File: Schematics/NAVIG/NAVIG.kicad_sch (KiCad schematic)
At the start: 19 parts, among them J12 GNSS_SMA, U11 BMP390, U4 BNO055, U4 STM32F205RETx, U7 NEO-M9N, Y2 32.768KHz

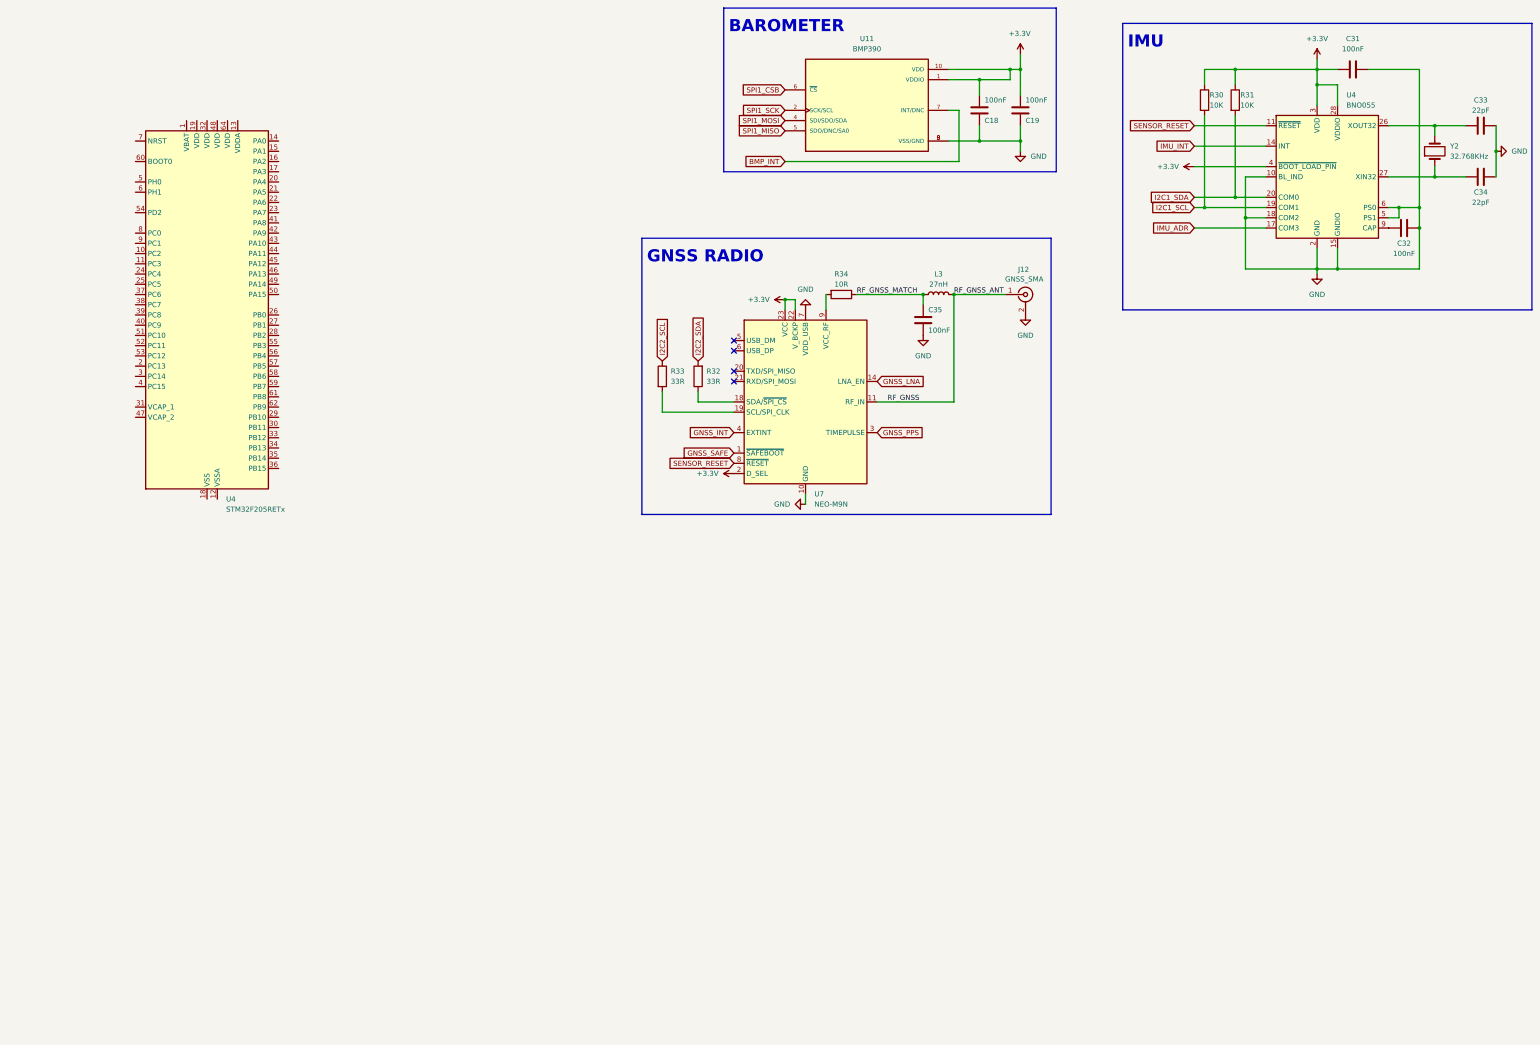
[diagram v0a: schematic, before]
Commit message: navig board pcb and schematic along with cntrl board edits
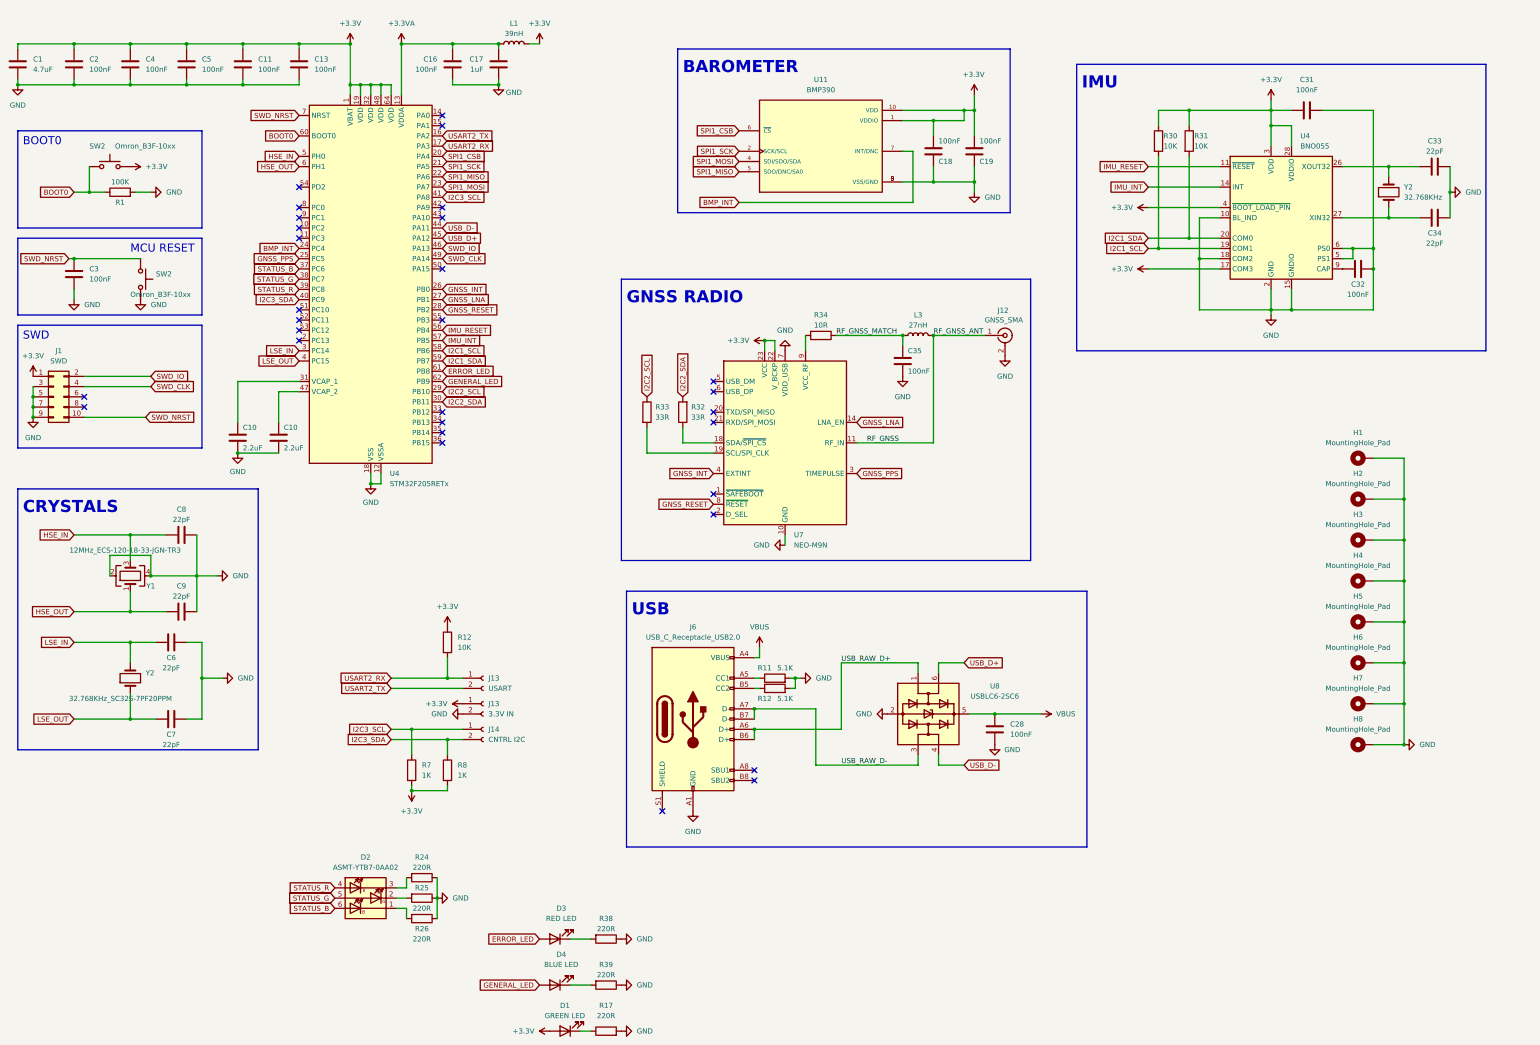
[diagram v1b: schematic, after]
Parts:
- added C1: 4.7uF, Capacitor_SMD:C_0603_1608Metric, symbol Device:C
- added C10 (x2): 2.2uF, Capacitor_SMD:C_0603_1608Metric, symbol Device:C
- added C11, C13, C16, C2, C28, C3, C4, C5: 100nF, Capacitor_SMD:C_0603_1608Metric, symbol Device:C
- added C17: 1uF, Capacitor_SMD:C_0603_1608Metric, symbol Device:C
- added C6, C7, C8, C9: 22pF, Capacitor_SMD:C_0603_1608Metric, symbol Device:C
- added D1: GREEN LED, LED_SMD:LED_0603_1608Metric, symbol Device:LED
- added D2: ASMT-YTB7-0AA02, LED_SMD:LED_Avago_PLCC6_3x2.8mm, symbol LED:ASMT-YTB7-0AA02
- added D3: RED LED, LED_SMD:LED_0603_1608Metric, symbol Device:LED
- added D4: BLUE LED, LED_SMD:LED_0603_1608Metric, symbol Device:LED
- added H1, H2, H3, H4, H5, H6, H7, H8: MountingHole_Pad, MountingHole:MountingHole_2.2mm_M2_Pad_TopBottom, symbol Mechanical:MountingHole_Pad
- added J1: SWD, Connector_PinHeader_1.27mm:PinHeader_2x05_P1.27mm_Vertical_SMD, symbol Connector_Generic:Conn_02x05_Odd_Even
- added J13: USART, Connector_JST:JST_XH_B2B-XH-A_1x02_P2.50mm_Vertical, symbol Connector:Conn_01x02_Socket
- added J13: 3.3V IN, Connector_JST:JST_XH_B2B-XH-A_1x02_P2.50mm_Vertical, symbol Connector:Conn_01x02_Socket
- added J14: CNTRL I2C, Connector_JST:JST_XH_B2B-XH-A_1x02_P2.50mm_Vertical, symbol Connector:Conn_01x02_Socket
- added J6: USB_C_Receptacle_USB2.0, Connector_USB:USB_C_Receptacle_GCT_USB4105-xx-A_16P_TopMnt_Horizontal, symbol Connector:USB_C_Receptacle_USB2.0
- added L1: 39nH, Inductor_SMD:L_0603_1608Metric, symbol Device:L
- added R1: 100K, Resistor_SMD:R_0603_1608Metric, symbol Device:R
- added R11, R12: 5.1K, Resistor_SMD:R_0603_1608Metric, symbol Device:R
- added R12: 10K, Resistor_SMD:R_0603_1608Metric, symbol Device:R
- added R17, R24, R25, R26, R38, R39: 220R, Resistor_SMD:R_0603_1608Metric, symbol Device:R
- added R7, R8: 1K, Resistor_SMD:R_0603_1608Metric, symbol Device:R
- added SW2 (x2): Omron_B3F-10xx, Button_Switch_THT:SW_TH_Tactile_Omron_B3F-10xx, symbol Switch:SW_Push
- added U8: USBLC6-2SC6, Package_TO_SOT_SMD:SOT-23-6, symbol Power_Protection:USBLC6-2SC6
- added Y1: 12MHz_ECS-120-18-33-JGN-TR3, Crystal:Crystal_SMD_3225-4Pin_3.2x2.5mm, symbol Device:Crystal_GND24
- added Y2: 32.768KHz_SC32S-7PF20PPM, Crystal:Crystal_SMD_3215-2Pin_3.2x1.5mm, symbol Device:Crystal
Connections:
- net IMU_ADR is gone; now on net +3.3V: U4.17 (COM3)
- net +3.3V: now also U4.1 (VBAT), U4.19 (VDD), U4.32 (VDD), U4.48 (VDD), U4.64 (VDD), C1.1, C11.1, C13.1, C2.1, C4.1, C5.1, D1.2 (A), J1.1 (Pin_1), J13.1 (Pin_1), L1.1, R12.1, R7.2, R8.2, SW2.2; no longer U7.2 (D_SEL)
- net BMP_INT: now also U4.24 (PC4)
- net GND: now also U4.12 (VSSA), U4.18 (VSS), U4.63 (VSS), C1.2, C10.1, C10.1, C11.2, C13.2, C16.2, C17.2, C2.2, C28.2, C3.2, C4.2, C5.2, C6.2, C7.2, C8.1, C9.2, H1.1, H2.1, H3.1, H4.1, H5.1, H6.1, H7.1, H8.1, J1.3 (Pin_3), J1.5 (Pin_5), J1.7 (Pin_7), J1.9 (Pin_9), J13.2 (Pin_2), J6.A1 (GND), J6.A12 (GND), J6.B1 (GND), J6.B12 (GND), R1.2, R11.2, R12.2, R17.2, R24.1, R25.1, R26.1, R38.1, R39.1, SW2.2, U8.2 (GND), Y1.2, Y1.4
- net GNSS_INT: now also U4.26 (PB0)
- net GNSS_LNA: now also U4.27 (PB1)
- net GNSS_PPS: now also U4.25 (PC5)
- net I2C1_SCL: now also U4.58 (PB6)
- net I2C1_SDA: now also U4.59 (PB7)
- net I2C2_SCL: now also U4.29 (PB10)
- net I2C2_SDA: now also U4.30 (PB11)
- net IMU_INT: now also U4.57 (PB5)
- net SPI1_CSB: now also U4.20 (PA4)
- net SPI1_MISO: now also U4.22 (PA6)
- net SPI1_MOSI: now also U4.23 (PA7)
- net SPI1_SCK: now also U4.21 (PA5)
- net +3.3VA: now reaches U4.13 (VDDA)
- net +3.3VA: now also C16.1, C17.1, L1.2
- net USART2_TX: now reaches U4.16 (PA2)
- net USART2_TX: now also J13.2 (Pin_2)
- net USART2_RX: now reaches U4.17 (PA3)
- net USART2_RX: now also J13.1 (Pin_1), R12.2
- net GNSS_RESET: now reaches U4.28 (PB2)
- net GNSS_RESET: now also U7.8 (~{RESET})
- net LSE_IN: now reaches U4.3 (PC14)
- net LSE_IN: now also C6.1, Y2.2
- net at U4.31 (VCAP_1): now also C10.2
- net STATUS_B: now reaches U4.37 (PC6)
- net STATUS_B: now also D2.6 (AB)
- net STATUS_G: now reaches U4.38 (PC7)
- net STATUS_G: now also D2.5 (AG)
- net STATUS_R: now reaches U4.39 (PC8)
- net STATUS_R: now also D2.4 (AR)
- net LSE_OUT: now reaches U4.4 (PC15)
- net LSE_OUT: now also C7.1, Y2.1
- net I2C3_SDA: now reaches U4.40 (PC9)
- net I2C3_SDA: now also J14.2 (Pin_2), R8.1
- net I2C3_SCL: now reaches U4.41 (PA8)
- net I2C3_SCL: now also J14.1 (Pin_1), R7.1
- net USB_D-: now reaches U4.44 (PA11)
- net USB_D-: now also U8.4 (I/O2)
- net USB_D+: now reaches U4.45 (PA12)
- net USB_D+: now also U8.6 (I/O1)
- net SWD_IO: now reaches U4.46 (PA13)
- net SWD_IO: now also J1.2 (Pin_2)
- net at U4.47 (VCAP_2): now also C10.2
- net SWD_CLK: now reaches U4.49 (PA14)
- net SWD_CLK: now also J1.4 (Pin_4)
- net HSE_IN: now reaches U4.5 (PH0)
- net HSE_IN: now also C8.2, Y1.3
- net IMU_RESET: now reaches U4.56 (PB4)
- net IMU_RESET: now also U4.11 (~{RESET})
- net HSE_OUT: now reaches U4.6 (PH1)
- net HSE_OUT: now also C9.1, Y1.1
- net BOOT0: now reaches U4.60 (BOOT0)
- net BOOT0: now also R1.1, SW2.1
- net ERROR_LED: now reaches U4.61 (PB8)
- net ERROR_LED: now also D3.2 (A)
- net GENERAL_LED: now reaches U4.62 (PB9)
- net GENERAL_LED: now also D4.2 (A)
- net SWD_NRST: now reaches U4.7 (NRST)
- net SWD_NRST: now also C3.1, J1.10 (Pin_10), SW2.1
- net GNSS_SAFE: no longer names the net of U7.1 (~{SAFEBOOT})
- removed net SENSOR_RESET: U4.11 (~{RESET}), U7.8 (~{RESET})
- new net: D2.2 (KG), R25.2
- new net: D1.1 (K), R17.1
- new net: D2.3 (KR), R24.2
- new net: D2.1 (KB), R26.2
- new net: J6.A5 (CC1), R11.1
- new net: J6.B5 (CC2), R12.1
- new net: D4.1 (K), R39.2
- new net: D3.1 (K), R38.2
- new net USB_RAW_D+: J6.A6 (D+), J6.B6 (D+), U8.1 (I/O1)
- new net USB_RAW_D-: J6.A7 (D-), J6.B7 (D-), U8.3 (I/O2)
- new net VBUS: C28.1, J6.A4 (VBUS), J6.A9 (VBUS), J6.B4 (VBUS), J6.B9 (VBUS), U8.5 (VBUS)
- no-connect marks 4 -> 30
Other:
- note added: "BOOT0"
- note added: "CRYSTALS"
- note added: "MCU RESET"
- note added: "SWD"
- note added: "USB"
- moved on the sheet: C18, C19, C31, C32, C33, C34, C35, J12, L3, R30, R31, R32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

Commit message: NAVIG v1 fixes and some experimental CNTRL updates for v2
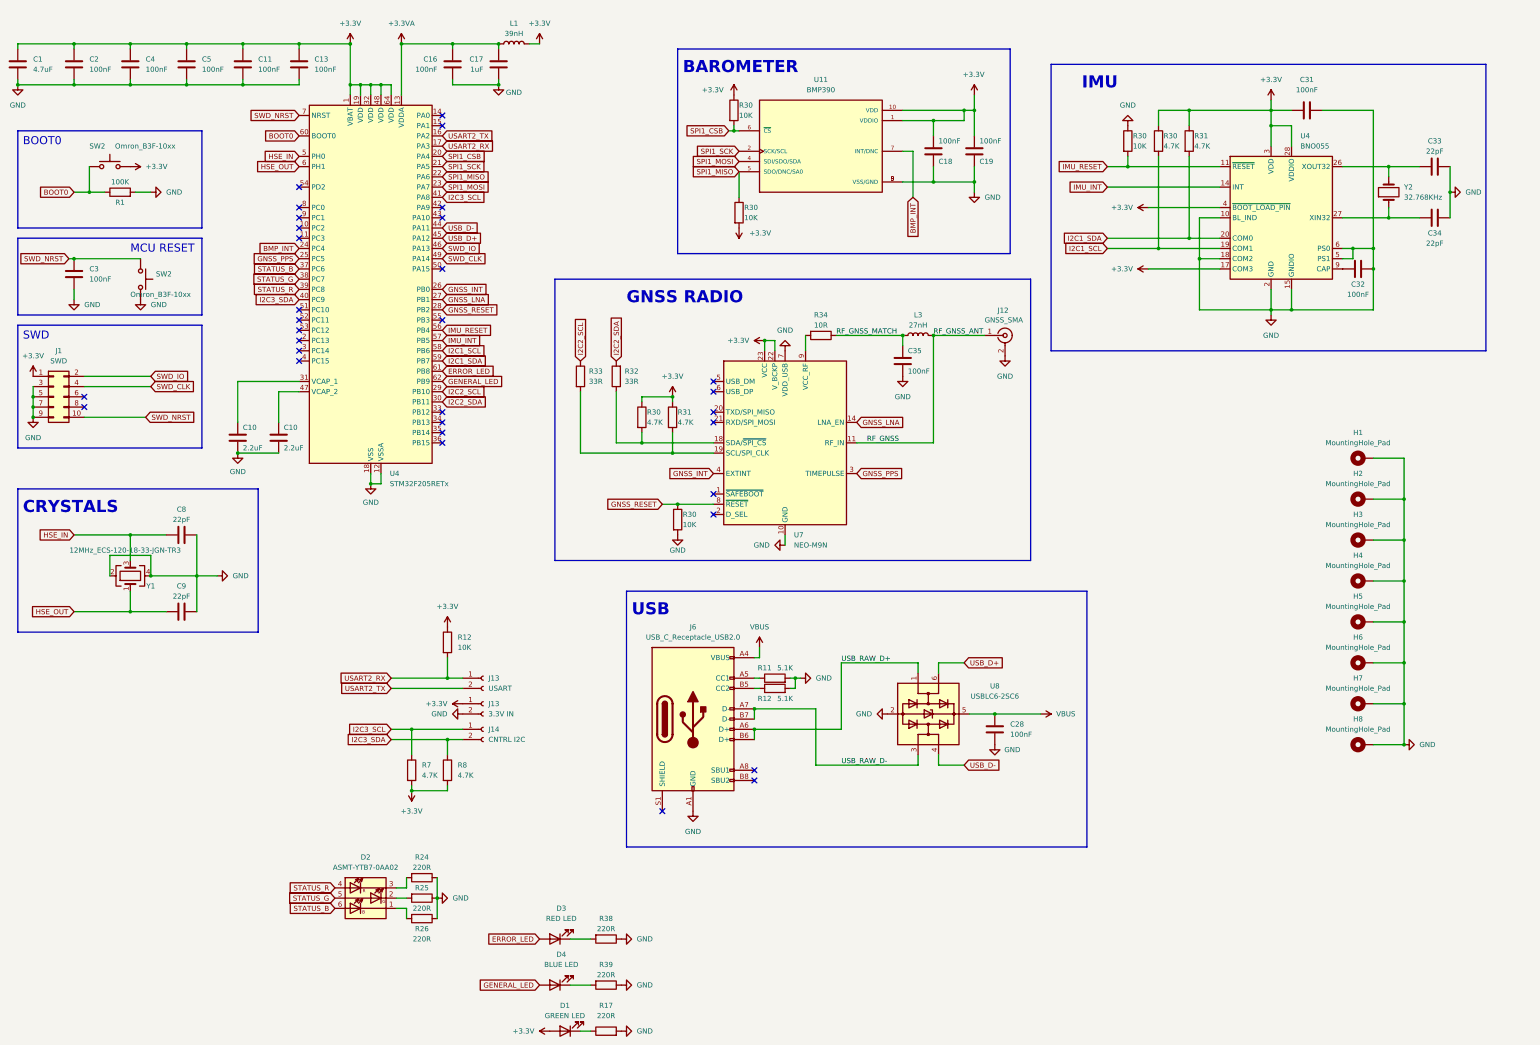
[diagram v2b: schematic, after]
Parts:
- removed C6, C7: 22pF, Capacitor_SMD:C_0603_1608Metric, symbol Device:C
- removed Y2: 32.768KHz_SC32S-7PF20PPM, Crystal:Crystal_SMD_3215-2Pin_3.2x1.5mm, symbol Device:Crystal
- added R30 (x4): 10K, Resistor_SMD:R_0603_1608Metric, symbol Device:R
- added R30, R31: 4.7K, Resistor_SMD:R_0603_1608Metric, symbol Device:R
- R30, R31: value 10K -> 4.7K
- R7, R8: value 1K -> 4.7K
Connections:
- net +3.3V: now also R30.1, R30.1, R30.2, R31.1
- net GND: now also R30.1, R30.2
- net GNSS_RESET: now also R30.1
- net IMU_RESET: now also R30.2
- net SPI1_CSB: now also R30.2
- net SPI1_MISO: now also R30.1
- net at R32.1, U7.18 (SDA/~{SPI_CS}): now also R30.2
- net at R33.2, U7.19 (SCL/SPI_CLK): now also R31.2
- net LSE_IN: no longer names the net of U4.3 (PC14)
- net LSE_OUT: no longer names the net of U4.4 (PC15)
- no-connect marks 30 -> 32
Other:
- moved on the sheet: R32, R33
